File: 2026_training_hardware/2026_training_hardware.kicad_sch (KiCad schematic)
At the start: 0 parts

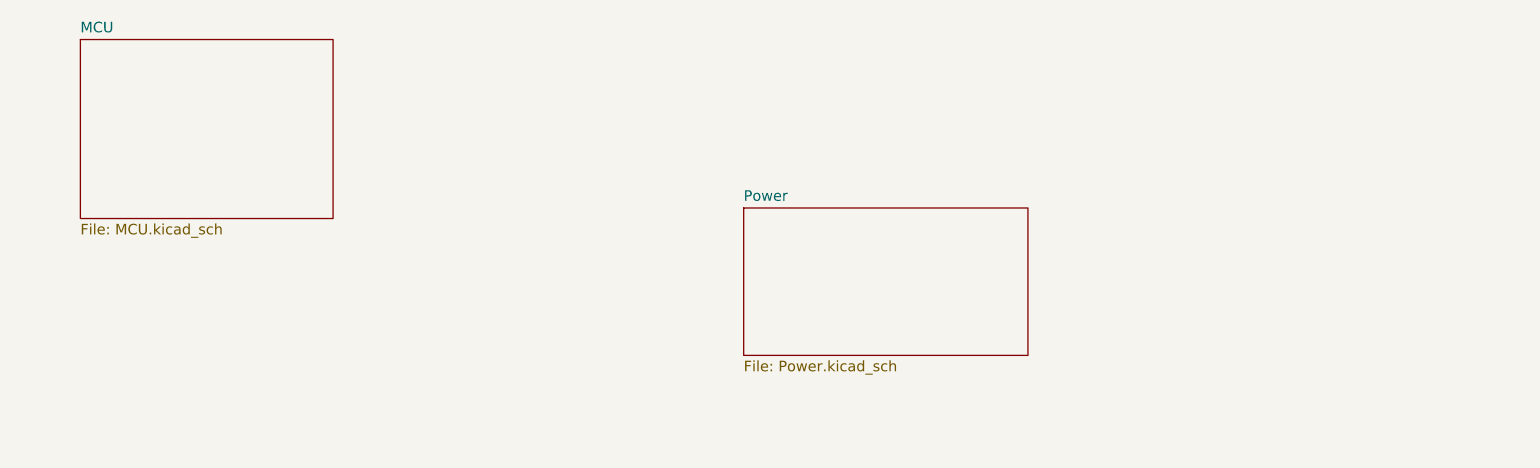
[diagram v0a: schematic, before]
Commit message: Add CAN
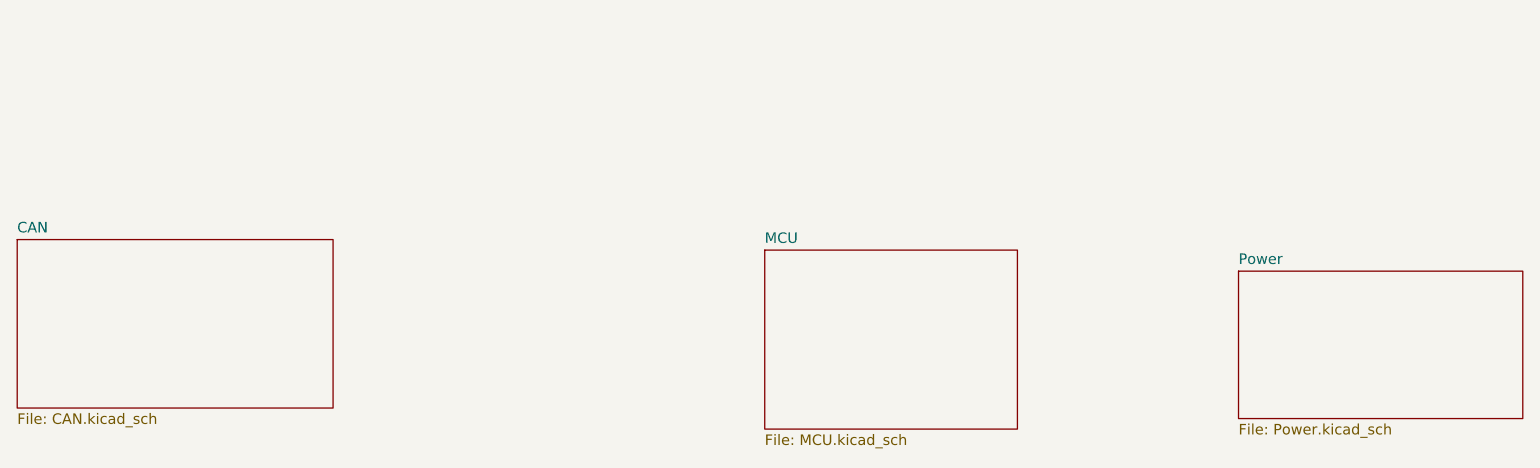
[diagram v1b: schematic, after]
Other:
- added sheet CAN (CAN.kicad_sch)
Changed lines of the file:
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@@
 	(paper "A4")
 	(sheet
-		(at 59.69 50.8)
+		(at 142.24 76.2)
 		(size 30.48 21.59)
 		(exclude_from_sim no)
@@
 		)
 		(property "Sheetname" "MCU"
-			(at 59.69 50.0884 0)
+			(at 142.24 75.4884 0)
 			(effects
 				(font
@@
 		)
 		(property "Sheetfile" "MCU.kicad_sch"
-			(at 59.69 72.9746 0)
+			(at 142.24 98.3746 0)
 			(effects
 				(font
@@
 	)
 	(sheet
-		(at 139.7 71.12)
+		(at 199.39 78.74)
 		(size 34.29 17.78)
 		(exclude_from_sim no)
@@
 		)
 		(property "Sheetname" "Power"
-			(at 139.7 70.4084 0)
+			(at 199.39 78.0284 0)
 			(effects
 				(font
@@
 		)
 		(property "Sheetfile" "Power.kicad_sch"
-			(at 139.7 89.4846 0)
+			(at 199.39 97.1046 0)
 			(effects
 				(font
@@
 				)
 			)
+		)
+	)
+	(sheet
+		(at 52.07 74.93)
+		(size 38.1 20.32)
+		(exclude_from_sim no)
+		(in_bom yes)
+		(on_board yes)
+		(dnp no)
+		(fields_autoplaced yes)
+		(stroke
+			(width 0.1524)
+			(type solid)
+		)
+		(fill
+			(color 0 0 0 0.0000)
+		)
+		(property "Sheetname" "CAN"
+			(at 52.07 74.2184 0)
+			(effects
+				(font
+					(size 1.27 1.27)
+				)
+				(justify left bottom)
+			)
+		)
+		(property "Sheetfile" "CAN.kicad_sch"
+			(at 52.07 95.8346 0)
+			(effects
+				(font
+					(size 1.27 1.27)
+				)
+				(justify left top)
+			)
+		)
+		(instances
+			(project "2026_training_hardware"
+				(path "/396efc46-0624-4b5a-8d52-10436ddb56f1"
+					(page "4")
+				)
+			)

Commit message: Finish Schematic
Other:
- sheet CAN ports: added RXD, STBY, TXD; removed none
- sheet MCU ports: added CRX1, CTX1, STBY; removed none
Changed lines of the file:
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@@
 	(generator_version "9.0")
 	(paper "A4")
+	(wire
+		(pts
+			(xy 90.17 88.9) (xy 106.68 88.9)
+		)
+		(stroke
+			(width 0)
+			(type default)
+		)
+	)
+	(wire
+		(pts
+			(xy 90.17 83.82) (xy 106.68 83.82)
+		)
+		(stroke
+			(width 0)
+			(type default)
+		)
+	)
+	(wire
+		(pts
+			(xy 90.17 80.01) (xy 106.68 80.01)
+		)
+		(stroke
+			(width 0)
+			(type default)
+		)
+	)
 	(sheet
-		(at 142.24 76.2)
+		(at 106.68 74.93)
 		(size 30.48 21.59)
 		(exclude_from_sim no)
@@
 		)
 		(property "Sheetname" "MCU"
-			(at 142.24 75.4884 0)
+			(at 106.68 74.2184 0)
 			(effects
 				(font
@@
 		)
 		(property "Sheetfile" "MCU.kicad_sch"
-			(at 142.24 98.3746 0)
+			(at 106.68 97.1046 0)
 			(effects
 				(font
@@
 				)
 				(justify left top)
+			)
+		)
+		(pin "CRX1" input
+			(at 106.68 88.9 180)
+			(effects
+				(font
+					(size 1.27 1.27)
+				)
+				(justify left)
+			)
+		)
+		(pin "CTX1" output
+			(at 106.68 80.01 180)
+			(effects
+				(font
+					(size 1.27 1.27)
+				)
+				(justify left)
+			)
+		)
+		(pin "STBY" output
+			(at 106.68 83.82 180)
+			(effects
+				(font
+					(size 1.27 1.27)
+				)
+				(justify left)
 			)
 		)
@@
 			)
 		)
+		(pin "RXD" output
+			(at 90.17 88.9 0)
+			(effects
+				(font
+					(size 1.27 1.27)
+				)
+				(justify right)
+			)
+		)
+		(pin "STBY" input
+			(at 90.17 83.82 0)
+			(effects
+				(font
+					(size 1.27 1.27)
+				)
+				(justify right)
+			)
+		)
+		(pin "TXD" input
+			(at 90.17 80.01 0)
+			(effects
+				(font
+					(size 1.27 1.27)
+				)
+				(justify right)
+			)
+		)
